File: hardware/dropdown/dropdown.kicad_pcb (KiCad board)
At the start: 2 copper layers, 20.8 x 10 mm, 14 parts, among them J1 12, J2 G, J3 3, J4 G, J5 12, J6 G, J7 3, J8 G, T1 T1, T2 T2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

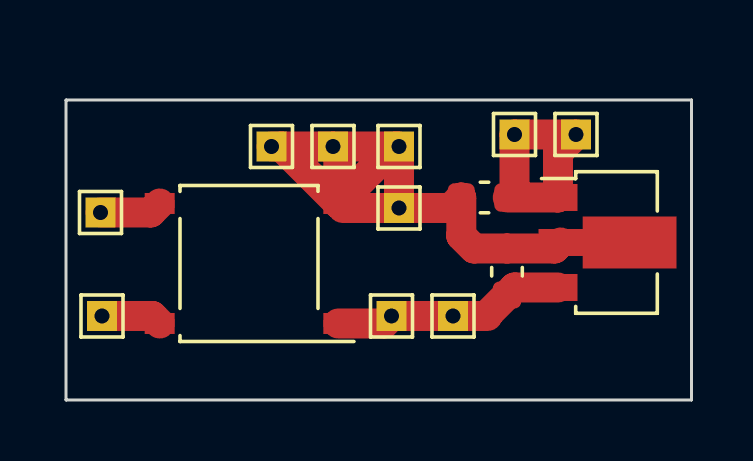
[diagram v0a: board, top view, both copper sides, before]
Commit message: feat: 4 layers PCB + AMS1117 (#17)
* feat: drop down 4 layer

* ams1117
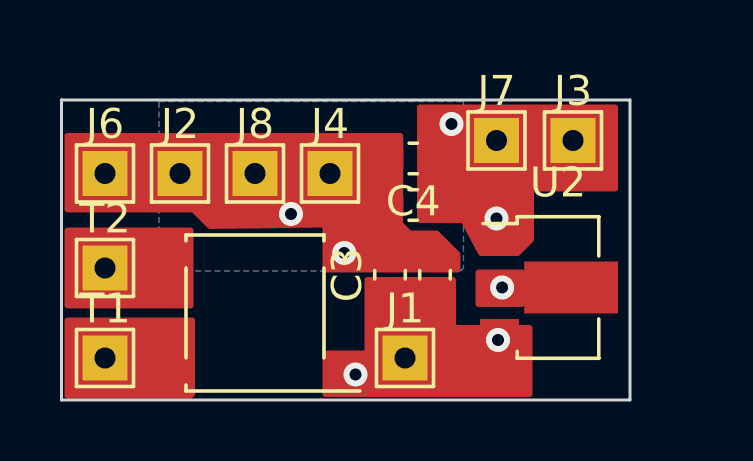
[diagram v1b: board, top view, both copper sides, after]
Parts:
- removed J5: 12, TestPoint:TestPoint_THTPad_1.0x1.0mm_Drill0.5mm
- added C3: 100nF, Capacitor_SMD:C_0603_1608Metric, F.Cu at (83.8, 64.1)
- added C4: 100nF, Capacitor_SMD:C_0603_1608Metric, F.Cu at (84.5, 60.2)
- J1, J2, J3, J4, J6, J7, J8, T1, T2: footprint TestPoint:TestPoint_THTPad_1.0x1.0mm_Drill0.5mm -> TestPoint:TestPoint_THTPad_1.5x1.5mm_Drill0.7mm
- U2: value AP7381-33Y-13 -> AMS1117-3.3
- moved J6 9.87 mm to (74.2, 60.7)
- moved J2 3.18 mm to (76.8, 60.7)
- moved J8 2.75 mm to (79.2, 60.7)
- moved J4 2.47 mm to (81.8, 60.7)
- moved U2 2.46 mm to (89.3, 64.5)
- moved C2 2.40 mm to (85.2, 64.1)
- moved C1 2.39 mm to (84.5, 61.8)
- moved T2 1.86 mm to (74.2, 63.9)
- moved D3 1.66 mm to (79.2, 65.3)
- moved J1 1.47 mm to (84.2, 66.8)
- moved T1 1.40 mm to (74.2, 66.8)
- moved J7 0.63 mm to (87.3, 59.6)
- moved J3 0.22 mm to (89.8, 59.6)
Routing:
- net GND: track 23.2 -> 0.00 mm, vias 0 -> 3
- net +3.3V: track 8.27 -> 0.00 mm, vias 0 -> 2
- net VD: track 7.85 -> 0.00 mm, vias 0 -> 2
- net GND1: track 2.10 -> 0.00 mm
- net +12V: track 2.03 -> 0.00 mm
- added copper zone on In2.Cu, net +12V
- added copper zone on In1.Cu, net +3.3V
- added copper zone on B.Cu, net GND
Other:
- board size 20.8 x 10 mm -> 19 x 10 mm
- copper layers 2 -> 4
